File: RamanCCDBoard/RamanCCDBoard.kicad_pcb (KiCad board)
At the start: 2 copper layers, 61 x 15.2 mm, 9 parts, among them J1 Conn_01x03_Pin, U1 ILX511

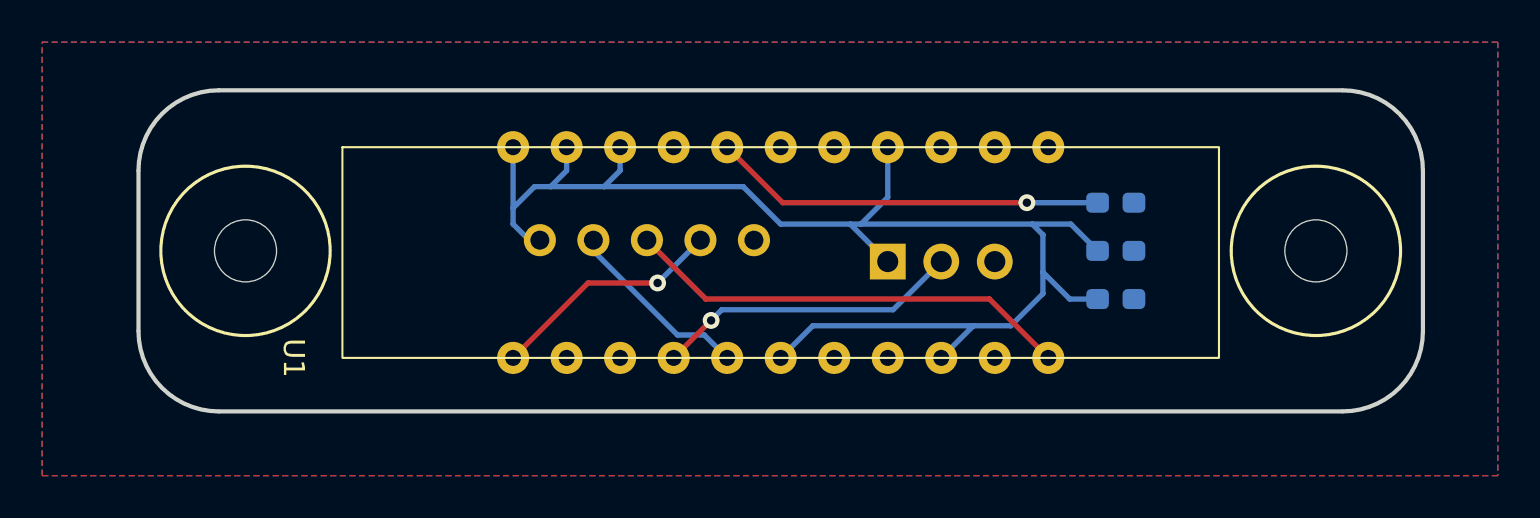
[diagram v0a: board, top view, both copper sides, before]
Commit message: add bjt to ccd
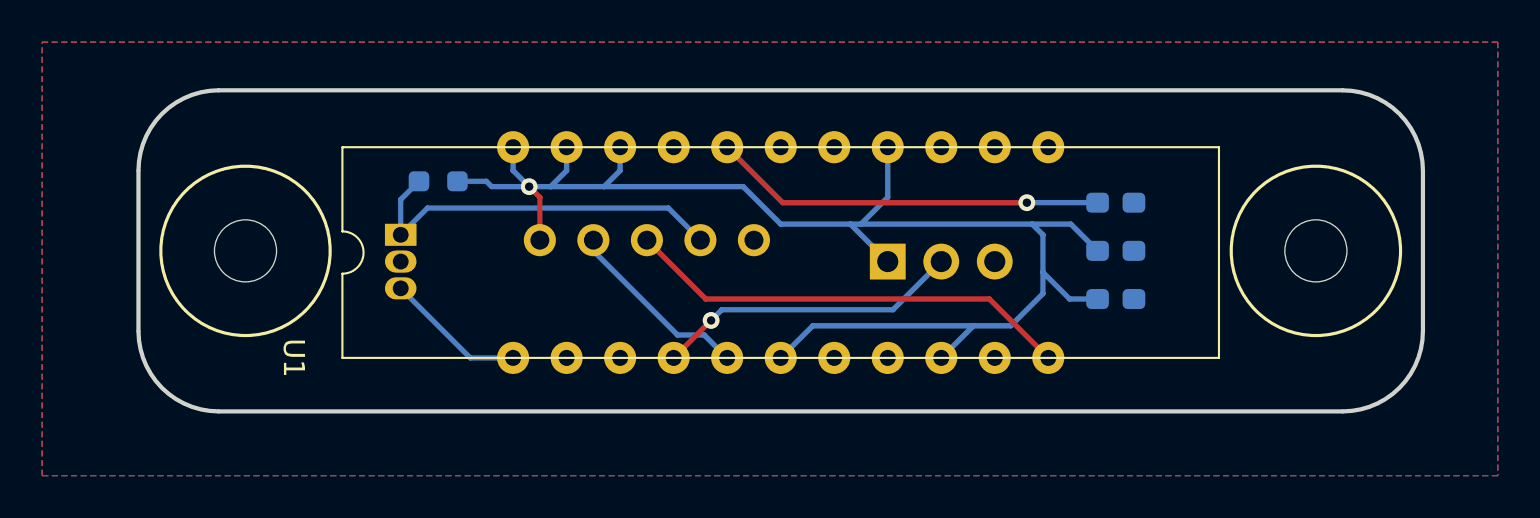
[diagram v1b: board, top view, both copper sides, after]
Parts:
- added Q2: KSA1015YTA, Package_TO_SOT_THT:TO-92_Inline, B.Cu at (50.3, 26.2)
- added R1: 3.0k, Resistor_SMD:R_0603_1608Metric_Pad0.98x0.95mm_HandSolder, B.Cu at (52.1, 23.6)
- moved G*** 17.9 mm to (78.2, 42.2)
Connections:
- U1 pad 1: Vout -> BJT_Input
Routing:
- net Vout: track 11.2 -> 18.3 mm, vias 1 -> 0
- net BJT_Input: track 0.00 -> 6.70 mm
- net +5V: track 68.4 -> 70.2 mm, vias 0 -> 1
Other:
- board text added: "CCD Breakout, Rev2 Mars Rover Design Team Missouri S&T, 2024 Caleb Ehlers"
- board text removed: "CCD Breakout, Rev1 Mars Rover Design Team Missouri S&T, 2024 Caleb Ehlers"

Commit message: change pin ordering for ccd molex
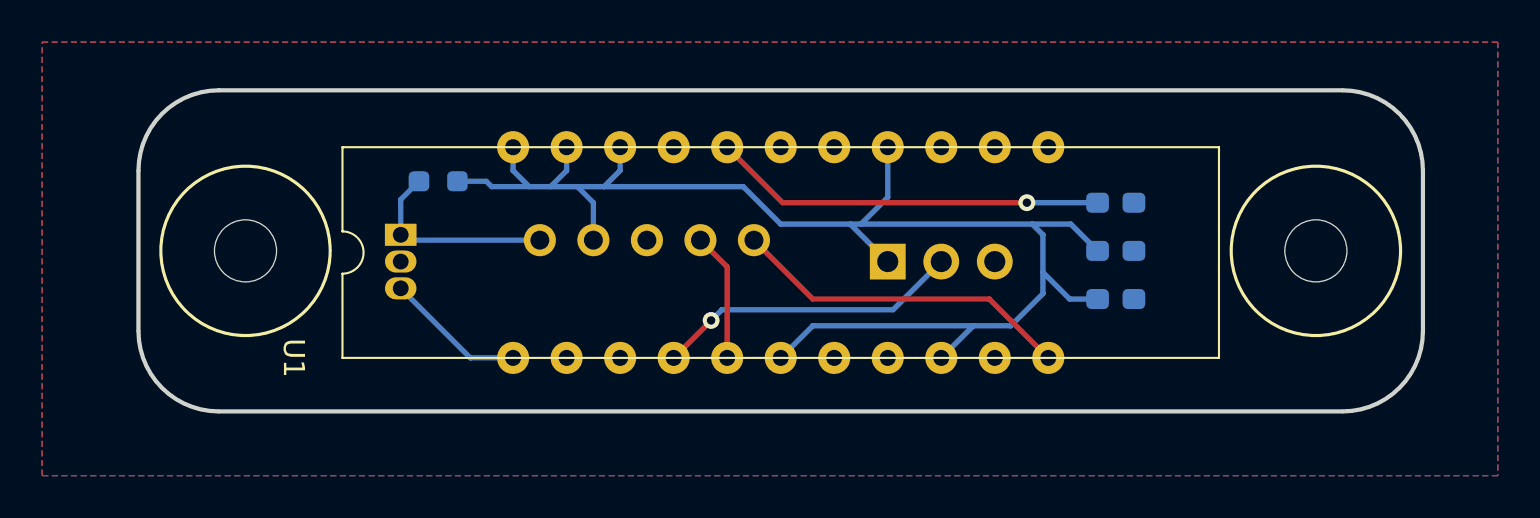
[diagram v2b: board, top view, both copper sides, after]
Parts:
- R1: value 3.0k -> 6.8k
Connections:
- Conn1 pad 1: +5V -> Vout
- Conn1 pad 2: øCLK -> +5V
- Conn1 pad 3: øROG -> GND
- Conn1 pad 4: Vout -> øCLK
- Conn1 pad 5: GND -> øROG
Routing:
- net Vout: track 18.3 -> 9.61 mm
- net øROG: track 21.4 -> 16.3 mm
- net øCLK: track 8.45 -> 6.11 mm
- net +5V: track 70.2 -> 70.4 mm, vias 1 -> 0
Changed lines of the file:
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@@
         (effects (font (size 1 1) (thickness 0.15)) (justify mirror))
     )
-    (fp_text value "3.0k" (at 0 -1.43) (layer "B.Fab")
+    (fp_text value "6.8k" (at 0 -1.43) (layer "B.Fab")
         (effects (font (size 1 1) (thickness 0.15)) (justify mirror))
     )
@@
       (stroke (width 0.15) (type solid)) (layer "B.SilkS"))
     (pad "1" thru_hole circle (at 0 0) (size 1.524 1.524) (drill 0.9) (layers "*.Cu" "*.Mask")
+      (net 5 "Vout") (pintype "input"))
+    (pad "2" thru_hole circle (at 2.54 0) (size 1.524 1.524) (drill 0.9) (layers "*.Cu" "*.Mask")
       (net 3 "+5V") (pintype "input"))
-    (pad "2" thru_hole circle (at 2.54 0) (size 1.524 1.524) (drill 0.9) (layers "*.Cu" "*.Mask")
+    (pad "3" thru_hole circle (at 5.08 0) (size 1.524 1.524) (drill 0.9) (layers "*.Cu" "*.Mask")
+      (net 1 "GND") (pintype "input"))
+    (pad "4" thru_hole circle (at 7.62 0) (size 1.524 1.524) (drill 0.9) (layers "*.Cu" "*.Mask")
       (net 6 "øCLK") (pintype "input"))
-    (pad "3" thru_hole circle (at 5.08 0) (size 1.524 1.524) (drill 0.9) (layers "*.Cu" "*.Mask")
+    (pad "5" thru_hole circle (at 10.16 0) (size 1.524 1.524) (drill 0.9) (layers "*.Cu" "*.Mask")
       (net 10 "øROG") (pintype "input"))
-    (pad "4" thru_hole circle (at 7.62 0) (size 1.524 1.524) (drill 0.9) (layers "*.Cu" "*.Mask")
-      (net 5 "Vout") (pintype "input"))
-    (pad "5" thru_hole circle (at 10.16 0) (size 1.524 1.524) (drill 0.9) (layers "*.Cu" "*.Mask")
-      (net 1 "GND") (pintype "input"))
     (model "${MRDT_KICAD_LIBRARIES}/3D Files/MRDT_Connctors/Molex_SL_05_Vertical.stp"
       (offset (xyz -2.539999962 -2.539999962 13.3349998))
@@
   (via (at 80.01 24.638) (size 0.8) (drill 0.4) (layers "F.Cu" "B.Cu") (net 2))
   (segment (start 83.365 24.638) (end 80.01 24.638) (width 0.254) (layer "B.Cu") (net 2))
-  (segment (start 56.388 23.876) (end 56.896 24.384) (width 0.25) (layer "F.Cu") (net 3))
-  (segment (start 56.896 24.384) (end 56.896 26.416) (width 0.25) (layer "F.Cu") (net 3))
-  (via (at 56.388 23.876) (size 0.8) (drill 0.4) (layers "F.Cu" "B.Cu") (net 3))
+  (segment (start 58.674 23.876) (end 59.944 23.876) (width 0.254) (layer "B.Cu") (net 3))
   (segment (start 80.772 26.162) (end 80.772 27.94) (width 0.254) (layer "B.Cu") (net 3))
   (segment (start 80.772 27.94) (end 80.772 28.956) (width 0.254) (layer "B.Cu") (net 3))
@@
   (segment (start 75.946 32.004) (end 77.47 30.48) (width 0.254) (layer "B.Cu") (net 3))
   (segment (start 52.9825 23.622) (end 54.356 23.622) (width 0.25) (layer "B.Cu") (net 3))
-  (segment (start 57.404 23.876) (end 59.944 23.876) (width 0.254) (layer "B.Cu") (net 3))
   (segment (start 60.706 23.114) (end 59.944 23.876) (width 0.254) (layer "B.Cu") (net 3))
   (segment (start 73.406 27.432) (end 71.628 25.654) (width 0.254) (layer "B.Cu") (net 3))
@@
   (segment (start 79.248 30.48) (end 77.47 30.48) (width 0.254) (layer "B.Cu") (net 3))
   (segment (start 73.406 24.384) (end 72.136 25.654) (width 0.254) (layer "B.Cu") (net 3))
+  (segment (start 57.404 23.876) (end 58.674 23.876) (width 0.254) (layer "B.Cu") (net 3))
   (segment (start 82.095 25.654) (end 83.365 26.924) (width 0.254) (layer "B.Cu") (net 3))
   (segment (start 80.772 28.956) (end 79.248 30.48) (width 0.254) (layer "B.Cu") (net 3))
@@
   (segment (start 82.042 29.21) (end 83.365 29.21) (width 0.254) (layer "B.Cu") (net 3))
   (segment (start 68.326 25.654) (end 71.628 25.654) (width 0.254) (layer "B.Cu") (net 3))
+  (segment (start 59.436 24.638) (end 58.674 23.876) (width 0.25) (layer "B.Cu") (net 3))
   (segment (start 58.166 23.114) (end 57.404 23.876) (width 0.254) (layer "B.Cu") (net 3))
   (segment (start 80.772 27.94) (end 82.042 29.21) (width 0.254) (layer "B.Cu") (net 3))
   (segment (start 57.404 23.876) (end 56.388 23.876) (width 0.254) (layer "B.Cu") (net 3))
+  (segment (start 59.436 26.416) (end 59.436 24.638) (width 0.25) (layer "B.Cu") (net 3))
   (segment (start 66.548 23.876) (end 68.326 25.654) (width 0.254) (layer "B.Cu") (net 3))
   (segment (start 73.406 22.004) (end 73.406 24.384) (width 0.254) (layer "B.Cu") (net 3))
@@
   (segment (start 65.532 29.718) (end 73.66 29.718) (width 0.254) (layer "B.Cu") (net 4))
   (segment (start 50.292 26.162) (end 50.292 24.4875) (width 0.25) (layer "B.Cu") (net 5))
-  (segment (start 64.516 26.416) (end 62.992 24.892) (width 0.25) (layer "B.Cu") (net 5))
+  (segment (start 56.896 26.416) (end 50.546 26.416) (width 0.25) (layer "B.Cu") (net 5))
   (segment (start 50.292 24.4875) (end 51.1575 23.622) (width 0.25) (layer "B.Cu") (net 5))
-  (segment (start 51.562 24.892) (end 50.292 26.162) (width 0.25) (layer "B.Cu") (net 5))
-  (segment (start 62.992 24.892) (end 51.562 24.892) (width 0.25) (layer "B.Cu") (net 5))
-  (segment (start 63.429 30.917) (end 64.699 30.917) (width 0.254) (layer "B.Cu") (net 6))
-  (segment (start 64.699 30.917) (end 65.786 32.004) (width 0.254) (layer "B.Cu") (net 6))
-  (segment (start 59.436 26.924) (end 63.429 30.917) (width 0.254) (layer "B.Cu") (net 6))
-  (segment (start 64.77 29.21) (end 61.976 26.416) (width 0.254) (layer "F.Cu") (net 10))
+  (segment (start 50.546 26.416) (end 50.292 26.162) (width 0.25) (layer "B.Cu") (net 5))
+  (segment (start 64.516 26.416) (end 65.786 27.686) (width 0.25) (layer "F.Cu") (net 6))
+  (segment (start 65.786 27.686) (end 65.786 32.004) (width 0.25) (layer "F.Cu") (net 6))
+  (segment (start 78.232 29.21) (end 69.85 29.21) (width 0.254) (layer "F.Cu") (net 10))
   (segment (start 81.026 32.004) (end 78.232 29.21) (width 0.254) (layer "F.Cu") (net 10))
-  (segment (start 78.232 29.21) (end 64.77 29.21) (width 0.254) (layer "F.Cu") (net 10))
+  (segment (start 67.056 26.416) (end 69.85 29.21) (width 0.25) (layer "F.Cu") (net 10))
   (segment (start 50.292 28.702) (end 53.594 32.004) (width 0.25) (layer "B.Cu") (net 13))
   (segment (start 53.594 32.004) (end 55.626 32.004) (width 0.25) (layer "B.Cu") (net 13))

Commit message: misc cleanup
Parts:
- removed G***: LOGO, Signatures:Caleb_Ehlers_Signature_15mmx4.8mm
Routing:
- net GND: vias 0 -> 1

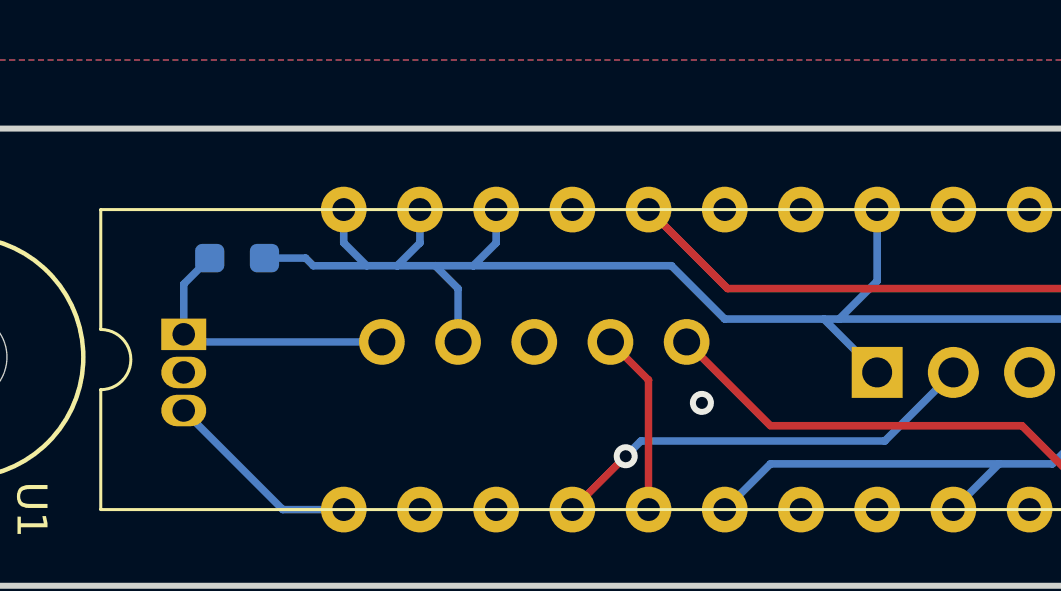
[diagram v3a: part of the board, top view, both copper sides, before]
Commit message: fix 5V traces
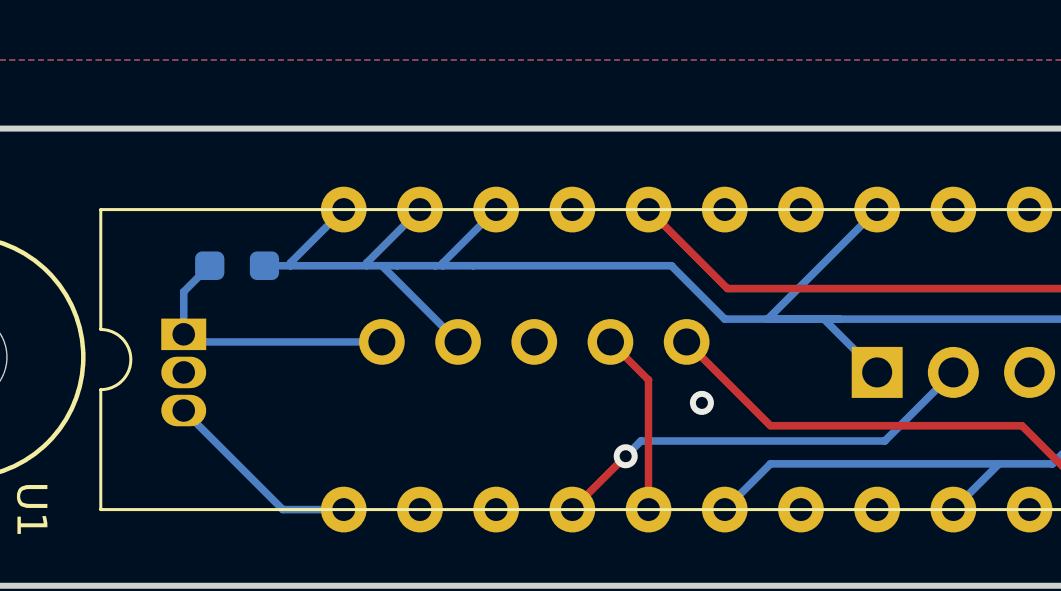
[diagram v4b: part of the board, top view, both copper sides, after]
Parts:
- moved R1 0.25 mm to (52.1, 23.9)
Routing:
- net +5V: track 70.4 -> 75.6 mm
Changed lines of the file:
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@@
   )
   (footprint "Resistor_SMD:R_0603_1608Metric_Pad0.98x0.95mm_HandSolder" (layer "B.Cu")
-    (at 52.07 23.622 180)
+    (at 52.07 23.876 180)
     (descr "Resistor SMD 0603 (1608 Metric), square (rectangular) end terminal, IPC_7351 nominal with elongated pad for handsoldering. (Body size source: IPC-SM-782 page 72, https://www.pcb-3d.com/wordpress/wp-content/uploads/ipc-sm-782a_amendment_1_and_2.pdf), generated with kicad-footprint-generator")
     (tags "resistor handsolder")
@@
   (via (at 80.01 24.638) (size 0.8) (drill 0.4) (layers "F.Cu" "B.Cu") (net 2))
   (segment (start 83.365 24.638) (end 80.01 24.638) (width 0.254) (layer "B.Cu") (net 2))
-  (segment (start 58.674 23.876) (end 59.944 23.876) (width 0.254) (layer "B.Cu") (net 3))
-  (segment (start 80.772 26.162) (end 80.772 27.94) (width 0.254) (layer "B.Cu") (net 3))
+  (segment (start 53.848 23.782) (end 53.848 23.876) (width 0.25) (layer "B.Cu") (net 3))
+  (segment (start 58.674 23.876) (end 58.928 23.876) (width 0.254) (layer "B.Cu") (net 3))
+  (segment (start 55.626 22.004) (end 53.848 23.782) (width 0.25) (layer "B.Cu") (net 3))
   (segment (start 80.772 27.94) (end 80.772 28.956) (width 0.254) (layer "B.Cu") (net 3))
-  (segment (start 54.356 23.622) (end 54.61 23.876) (width 0.25) (layer "B.Cu") (net 3))
+  (segment (start 56.388 23.782) (end 56.388 23.876) (width 0.25) (layer "B.Cu") (net 3))
   (segment (start 80.264 25.654) (end 80.772 26.162) (width 0.254) (layer "B.Cu") (net 3))
-  (segment (start 58.166 22.004) (end 58.166 23.114) (width 0.254) (layer "B.Cu") (net 3))
   (segment (start 75.946 32.004) (end 77.47 30.48) (width 0.254) (layer "B.Cu") (net 3))
-  (segment (start 52.9825 23.622) (end 54.356 23.622) (width 0.25) (layer "B.Cu") (net 3))
-  (segment (start 60.706 23.114) (end 59.944 23.876) (width 0.254) (layer "B.Cu") (net 3))
   (segment (start 73.406 27.432) (end 71.628 25.654) (width 0.254) (layer "B.Cu") (net 3))
   (segment (start 80.264 25.654) (end 82.095 25.654) (width 0.254) (layer "B.Cu") (net 3))
   (segment (start 77.47 30.48) (end 69.85 30.48) (width 0.254) (layer "B.Cu") (net 3))
+  (segment (start 59.436 26.416) (end 56.896 23.876) (width 0.25) (layer "B.Cu") (net 3))
+  (segment (start 52.9825 23.876) (end 53.848 23.876) (width 0.25) (layer "B.Cu") (net 3))
+  (segment (start 73.406 22.004) (end 69.756 25.654) (width 0.254) (layer "B.Cu") (net 3))
+  (segment (start 60.706 22.004) (end 58.928 23.782) (width 0.25) (layer "B.Cu") (net 3))
   (segment (start 79.248 30.48) (end 77.47 30.48) (width 0.254) (layer "B.Cu") (net 3))
-  (segment (start 73.406 24.384) (end 72.136 25.654) (width 0.254) (layer "B.Cu") (net 3))
+  (segment (start 58.166 22.004) (end 56.388 23.782) (width 0.25) (layer "B.Cu") (net 3))
+  (segment (start 56.896 23.876) (end 56.388 23.876) (width 0.254) (layer "B.Cu") (net 3))
   (segment (start 57.404 23.876) (end 58.674 23.876) (width 0.254) (layer "B.Cu") (net 3))
+  (segment (start 53.848 23.876) (end 56.388 23.876) (width 0.25) (layer "B.Cu") (net 3))
+  (segment (start 80.772 26.162) (end 80.772 27.94) (width 0.254) (layer "B.Cu") (net 3))
   (segment (start 82.095 25.654) (end 83.365 26.924) (width 0.254) (layer "B.Cu") (net 3))
   (segment (start 80.772 28.956) (end 79.248 30.48) (width 0.254) (layer "B.Cu") (net 3))
-  (segment (start 54.61 23.876) (end 56.388 23.876) (width 0.25) (layer "B.Cu") (net 3))
+  (segment (start 58.928 23.782) (end 58.928 23.876) (width 0.25) (layer "B.Cu") (net 3))
   (segment (start 82.042 29.21) (end 83.365 29.21) (width 0.254) (layer "B.Cu") (net 3))
   (segment (start 68.326 25.654) (end 71.628 25.654) (width 0.254) (layer "B.Cu") (net 3))
-  (segment (start 59.436 24.638) (end 58.674 23.876) (width 0.25) (layer "B.Cu") (net 3))
-  (segment (start 58.166 23.114) (end 57.404 23.876) (width 0.254) (layer "B.Cu") (net 3))
+  (segment (start 69.756 25.654) (end 72.136 25.654) (width 0.254) (layer "B.Cu") (net 3))
+  (segment (start 57.404 23.876) (end 56.896 23.876) (width 0.254) (layer "B.Cu") (net 3))
   (segment (start 80.772 27.94) (end 82.042 29.21) (width 0.254) (layer "B.Cu") (net 3))
-  (segment (start 57.404 23.876) (end 56.388 23.876) (width 0.254) (layer "B.Cu") (net 3))
-  (segment (start 59.436 26.416) (end 59.436 24.638) (width 0.25) (layer "B.Cu") (net 3))
+  (segment (start 58.928 23.876) (end 59.944 23.876) (width 0.254) (layer "B.Cu") (net 3))
   (segment (start 66.548 23.876) (end 68.326 25.654) (width 0.254) (layer "B.Cu") (net 3))
-  (segment (start 73.406 22.004) (end 73.406 24.384) (width 0.254) (layer "B.Cu") (net 3))
-  (segment (start 56.388 23.876) (end 55.626 23.114) (width 0.254) (layer "B.Cu") (net 3))
   (segment (start 69.85 30.48) (end 68.326 32.004) (width 0.254) (layer "B.Cu") (net 3))
-  (segment (start 60.706 22.004) (end 60.706 23.114) (width 0.254) (layer "B.Cu") (net 3))
-  (segment (start 55.626 23.114) (end 55.626 22.004) (width 0.254) (layer "B.Cu") (net 3))
   (segment (start 59.944 23.876) (end 66.548 23.876) (width 0.254) (layer "B.Cu") (net 3))
   (segment (start 72.136 25.654) (end 80.264 25.654) (width 0.254) (layer "B.Cu") (net 3))
@@
   (segment (start 73.66 29.718) (end 75.946 27.432) (width 0.254) (layer "B.Cu") (net 4))
   (segment (start 65.532 29.718) (end 73.66 29.718) (width 0.254) (layer "B.Cu") (net 4))
-  (segment (start 50.292 26.162) (end 50.292 24.4875) (width 0.25) (layer "B.Cu") (net 5))
   (segment (start 56.896 26.416) (end 50.546 26.416) (width 0.25) (layer "B.Cu") (net 5))
-  (segment (start 50.292 24.4875) (end 51.1575 23.622) (width 0.25) (layer "B.Cu") (net 5))
+  (segment (start 50.292 26.162) (end 50.292 24.7415) (width 0.25) (layer "B.Cu") (net 5))
   (segment (start 50.546 26.416) (end 50.292 26.162) (width 0.25) (layer "B.Cu") (net 5))
+  (segment (start 50.292 24.7415) (end 51.1575 23.876) (width 0.25) (layer "B.Cu") (net 5))
   (segment (start 64.516 26.416) (end 65.786 27.686) (width 0.25) (layer "F.Cu") (net 6))
   (segment (start 65.786 27.686) (end 65.786 32.004) (width 0.25) (layer "F.Cu") (net 6))
